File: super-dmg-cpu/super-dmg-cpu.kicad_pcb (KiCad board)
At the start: 2 copper layers, 83 x 78.5 mm, 61 parts, among them CN1 SCREEN, CN2 CART, CN3 BATTERY, CN4 BATTERY, P1 CART SHIELD GND PADS, P2 GND PAD, P3 GND PAD, P4 GND PAD, SW1 DPDT, U1 CPU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

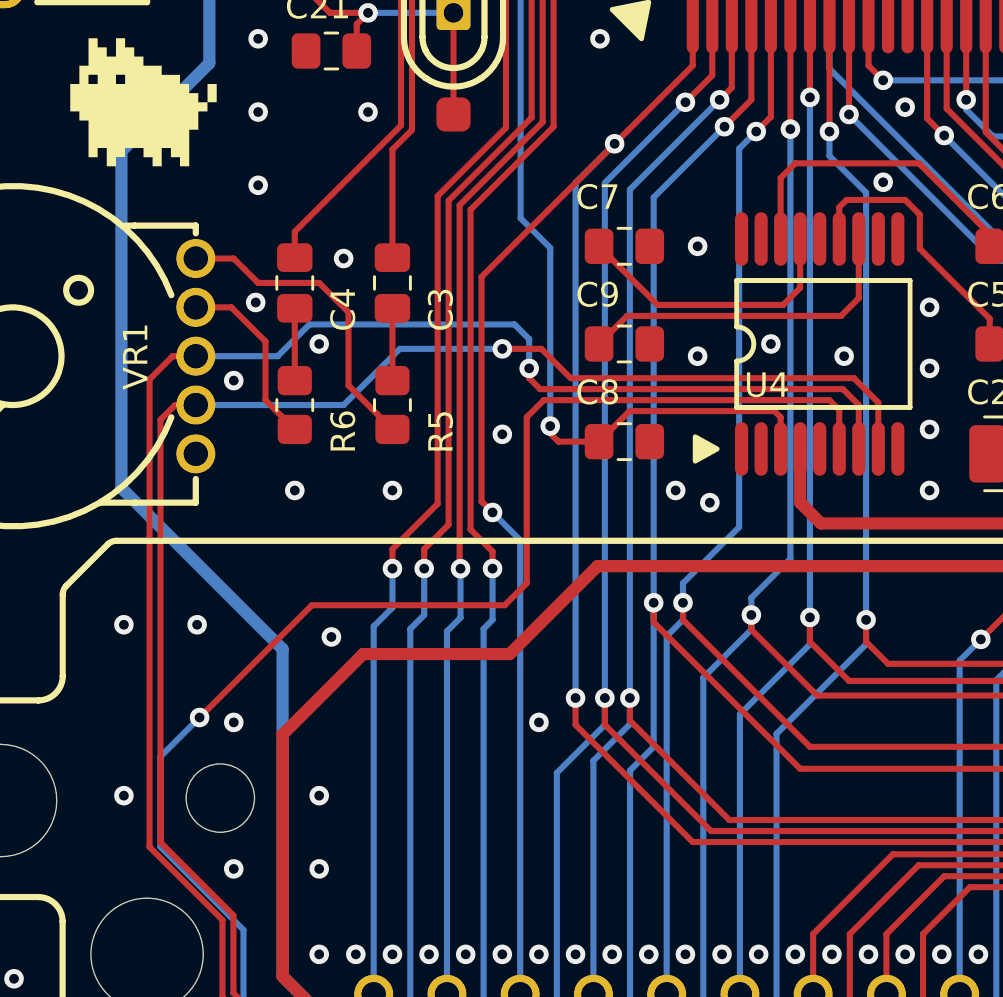
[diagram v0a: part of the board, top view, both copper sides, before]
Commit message: CPU: fix inverted L/R pins
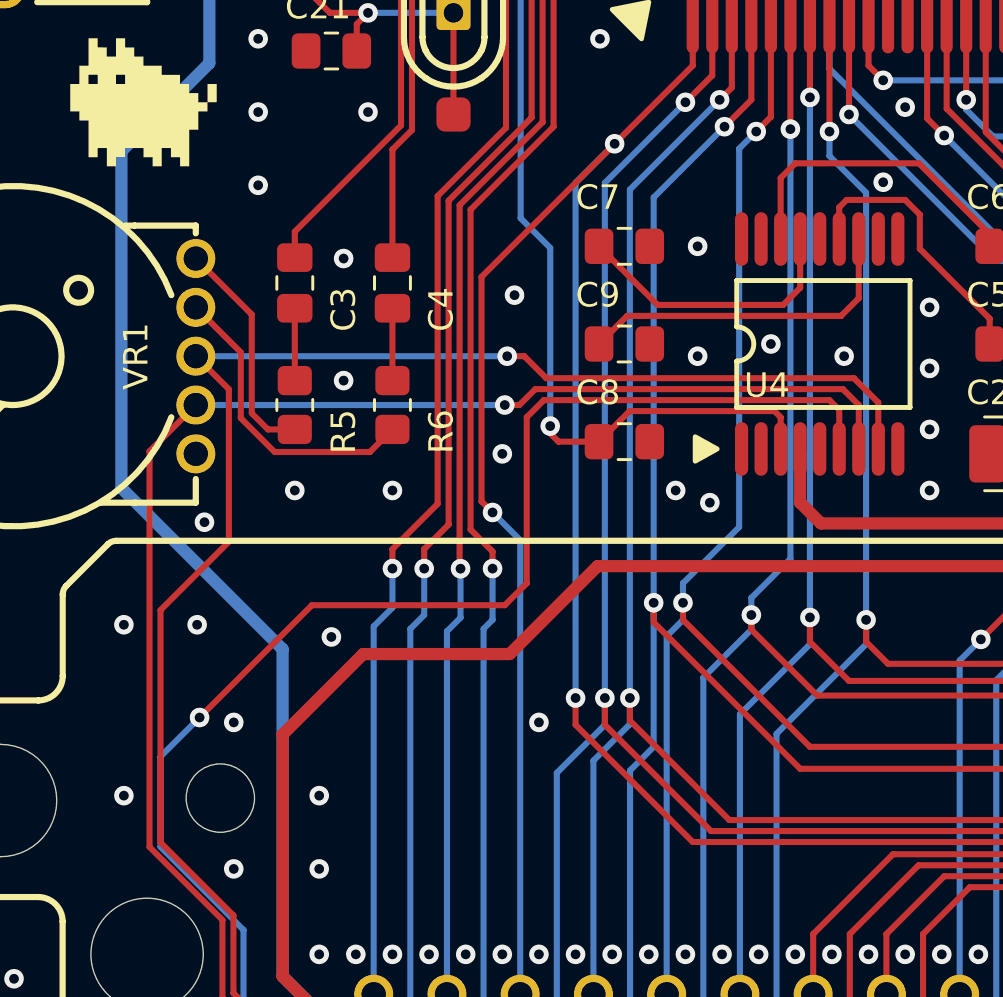
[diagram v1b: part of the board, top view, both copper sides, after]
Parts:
- moved C3 4.00 mm to (45.5, 67.5)
- moved C4 4.00 mm to (49.5, 67.5)
- moved R5 4.00 mm to (45.5, 72.5)
- moved R6 4.00 mm to (49.5, 72.5)
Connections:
- C3 pad 1: /LOUT -> /ROUT
- C4 pad 1: /ROUT -> /LOUT
- VR1 pad 2: /RPOT -> /LPOT
- VR1 pad 4: /LPOT -> /RPOT
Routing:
- net Net-(R6-Pad2): track 7.53 -> 12.5 mm
- net /RPOT: track 82.3 -> 77.5 mm
- net Net-(R5-Pad2): track 12.7 -> 9.32 mm
- net /LPOT: track 82.0 -> 83.5 mm

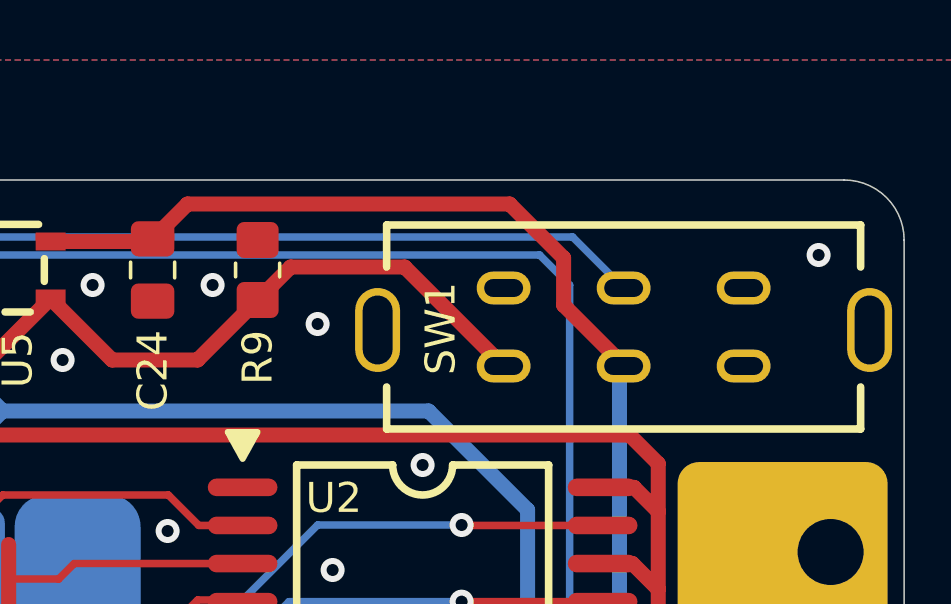
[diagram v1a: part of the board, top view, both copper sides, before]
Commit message: CPU: remove unused pads on the power switch
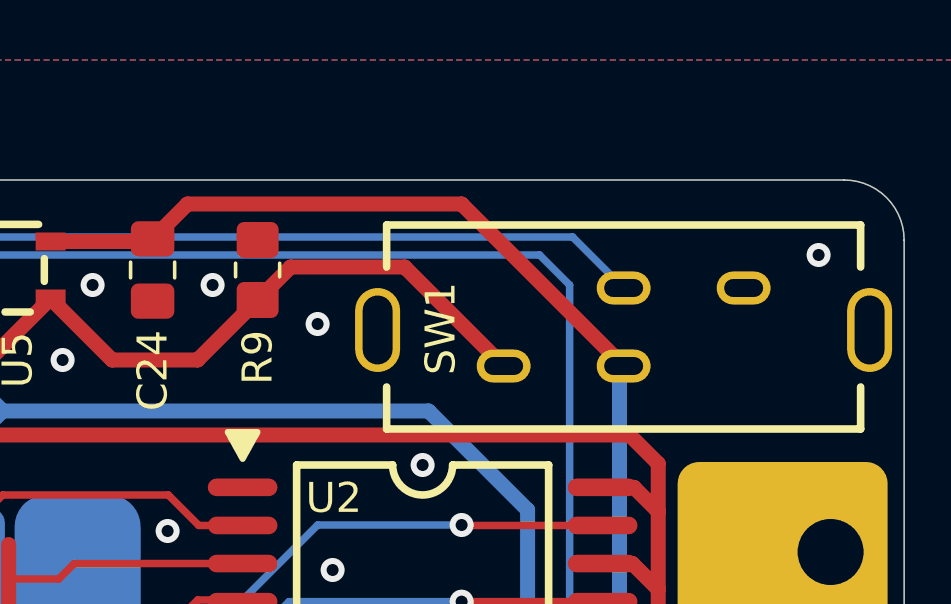
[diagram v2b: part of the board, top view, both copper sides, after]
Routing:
- net +BATT: track 182.2 -> 181.3 mm
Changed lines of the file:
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@@
   (net 109 "PD_OUT")
   (net 110 "unconnected-(U5-Pad3)")
-  (net 111 "unconnected-(SW1-Pad3)")
-  (net 112 "unconnected-(SW1-Pad4)")
-  (net 113 "Net-(D2-Pad1)")
+  (net 111 "Net-(D2-Pad1)")
   (footprint "dmg_lib:DMG_RAM_64K" locked (layer "F.Cu")
     (at 93.5 69.5)
@@
     (fp_line (start -5.5 -6.5) (end -5 -6.5) (layer "Dwgs.User") (width 0.254))
     (pad "1" thru_hole circle (at 0 -2.5) (size 1.4 1.4) (drill 0.8) (layers *.Mask "F.Cu" "In1.Cu" "B.Cu")
-      (net 113 "Net-(D2-Pad1)") (pinfunction "VDD") (pintype "passive"))
+      (net 111 "Net-(D2-Pad1)") (pinfunction "VDD") (pintype "passive"))
     (pad "2" thru_hole circle (at 2 -2.5) (size 1.4 1.4) (drill 0.8) (layers *.Mask "F.Cu" "In1.Cu" "B.Cu")
       (net 7 "/EXT_OUT") (pinfunction "SO") (pintype "passive"))
@@
     )
     (fp_line (start -7.9 -2.1) (end -7.9 -0.7) (layer "F.SilkS") (width 0.254))
-    (fp_line (start 7.9 -0.7) (end 7.9 -2.1) (layer "F.SilkS") (width 0.254))
-    (fp_line (start 7.9 -2.1) (end -7.9 -2.1) (layer "F.SilkS") (width 0.254))
     (fp_line (start -7.9 4.7) (end -7.9 3.3) (layer "F.SilkS") (width 0.254))
+    (fp_line (start 7.9 -2.1) (end -7.9 -2.1) (layer "F.SilkS") (width 0.254))
     (fp_line (start 7.9 4.7) (end 7.9 3.3) (layer "F.SilkS") (width 0.254))
+    (fp_line (start 7.9 -0.7) (end 7.9 -2.1) (layer "F.SilkS") (width 0.254))
     (fp_line (start -7.9 4.7) (end 7.9 4.7) (layer "F.SilkS") (width 0.254))
     (fp_line (start 5.4 -8.6) (end 5.4 -2.1) (layer "Dwgs.User") (width 0.25))
@@
     (pad "2" thru_hole oval locked (at 0 2.6) (size 1.8 1.1) (drill oval 1.3 0.6) (layers *.Cu *.Mask)
       (net 108 "+BATT") (pinfunction "VIN") (pintype "passive"))
-    (pad "3" thru_hole oval locked (at 4 2.6) (size 1.8 1.1) (drill oval 1.3 0.6) (layers *.Cu *.Mask)
-      (net 111 "unconnected-(SW1-Pad3)") (pinfunction "3") (pintype "no_connect"))
-    (pad "4" thru_hole oval locked (at -4 0) (size 1.8 1.1) (drill oval 1.3 0.6) (layers *.Cu *.Mask)
-      (net 112 "unconnected-(SW1-Pad4)") (pinfunction "4") (pintype "no_connect"))
     (pad "5" thru_hole oval locked (at 0 0) (size 1.8 1.1) (drill oval 1.3 0.6) (layers *.Cu *.Mask)
       (net 15 "/RST") (pinfunction "RST") (pintype "passive"))
     (pad "6" thru_hole oval locked (at 4 0) (size 1.8 1.1) (drill oval 1.3 0.6) (layers *.Cu *.Mask)
       (net 4 "GND") (pinfunction "GND") (pintype "passive"))
-    (pad "7" thru_hole oval locked (at 8.2 1.4 270) (size 2.8 1.5) (drill oval 2.3 1) (layers *.Cu *.Mask)
-      (net 4 "GND") (pinfunction "SH") (pintype "passive"))
     (pad "7" thru_hole oval locked (at -8.2 1.4 270) (size 2.8 1.5) (drill oval 2.3 1) (layers *.Cu *.Mask)
       (net 4 "GND") (pinfunction "SH") (pintype "passive"))
+    (pad "7" thru_hole oval locked (at 8.2 1.4 270) (size 2.8 1.5) (drill oval 2.3 1) (layers *.Cu *.Mask)
+      (net 4 "GND") (pinfunction "SH") (pintype "passive"))
   )
   (footprint "eda-glyphs:kmc_6mm" (layer "F.Cu")
@@
     (fp_line (start -1.4 -0.9) (end 1.4 -0.9) (layer "F.Fab") (width 0.1))
     (pad "1" smd rect (at -1.65 0 90) (size 0.9 1.2) (layers "F.Cu" "F.Paste" "F.Mask")
-      (net 113 "Net-(D2-Pad1)") (pinfunction "K") (pintype "passive"))
+      (net 111 "Net-(D2-Pad1)") (pinfunction "K") (pintype "passive"))
     (pad "2" smd rect (at 1.65 0 90) (size 0.9 1.2) (layers "F.Cu" "F.Paste" "F.Mask")
       (net 106 "+5V") (pinfunction "A") (pintype "passive"))
@@
     (fp_line (start -6 5) (end -5.031 5) (layer "F.SilkS") (width 0.254))
     (fp_arc (start -2.5 4) (mid -6.581538 -0.183962) (end -6 -6) (layer "F.SilkS") (width 0.254))
-    (fp_arc (start 6 -6) (mid 6.581539 -0.183962) (end 2.5 4) (layer "F.SilkS") (width 0.254))
+    (fp_arc (start 6 -6) (mid 6.581539 -0.183961) (end 2.5 4) (layer "F.SilkS") (width 0.254))
     (fp_arc (start -3.199638 -4.100525) (mid -3.096245 -5.695327) (end -1.501 -5.599) (layer "F.SilkS") (width 0.254))
     (fp_circle (center 0 -2.5) (end 2 -2.5) (layer "F.SilkS") (width 0.254) (fill none))
@@
   (segment (start 73.6 32) (end 79.55 32) (width 0.5) (layer "F.Cu") (net 107))
   (segment (start 32.05 101.35) (end 32.05 100) (width 0.5) (layer "F.Cu") (net 108))
-  (segment (start 98.7 28.6) (end 96.9 26.8) (width 0.5) (layer "F.Cu") (net 108))
   (segment (start 73.69 101.6) (end 71.297501 103.992499) (width 0.5) (layer "F.Cu") (net 108))
   (segment (start 102.525489 103.849511) (end 104.775 101.6) (width 0.5) (layer "F.Cu") (net 108))
-  (segment (start 96.9 26.8) (end 86.1625 26.8) (width 0.5) (layer "F.Cu") (net 108))
+  (segment (start 95.3 26.8) (end 86.1625 26.8) (width 0.5) (layer "F.Cu") (net 108))
   (segment (start 89.846569 102.742979) (end 88.576548 104.013) (width 0.5) (layer "F.Cu") (net 108))
-  (segment (start 86.1625 26.8) (end 85 27.9625) (width 0.5) (layer "F.Cu") (net 108))
+  (segment (start 100.668639 32.168639) (end 95.3 26.8) (width 0.5) (layer "F.Cu") (net 108))
   (segment (start 95.049547 102.742979) (end 96.156079 103.849511) (width 0.5) (layer "F.Cu") (net 108))
   (segment (start 92.436116 102.742979) (end 95.049547 102.742979) (width 0.5) (layer "F.Cu") (net 108))
+  (segment (start 86.1625 26.8) (end 85 27.9625) (width 0.5) (layer "F.Cu") (net 108))
   (segment (start 34.692499 103.992499) (end 32.05 101.35) (width 0.5) (layer "F.Cu") (net 108))
   (segment (start 76.103 104.013) (end 73.69 101.6) (width 0.5) (layer "F.Cu") (net 108))
   (segment (start 71.297501 103.992499) (end 34.692499 103.992499) (width 0.5) (layer "F.Cu") (net 108))
-  (segment (start 100.668639 32.139193) (end 98.7 30.170554) (width 0.5) (layer "F.Cu") (net 108))
-  (segment (start 98.7 30.170554) (end 98.7 28.6) (width 0.5) (layer "F.Cu") (net 108))
   (segment (start 81.6 28.05) (end 84.9125 28.05) (width 0.5) (layer "F.Cu") (net 108))
   (segment (start 92.436116 102.742979) (end 89.846569 102.742979) (width 0.5) (layer "F.Cu") (net 108))
+  (segment (start 100.668639 32.139193) (end 100.668639 32.168639) (width 0.5) (layer "F.Cu") (net 108))
   (segment (start 88.576548 104.013) (end 76.103 104.013) (width 0.5) (layer "F.Cu") (net 108))
   (segment (start 96.156079 103.849511) (end 102.525489 103.849511) (width 0.5) (layer "F.Cu") (net 108))
@@
   (segment (start 78 30.9) (end 78 31.7) (width 0.5) (layer "B.Cu") (net 109))
   (segment (start 97.5 37) (end 94.2 33.7) (width 0.5) (layer "B.Cu") (net 109))
-  (segment (start 35.95 47) (end 34.2 48.75) (width 0.25) (layer "F.Cu") (net 113))
-  (segment (start 34.2 48.75) (end 34.2 53.3) (width 0.25) (layer "F.Cu") (net 113))
-  (segment (start 36.05 55.15) (end 42 55.15) (width 0.25) (layer "F.Cu") (net 113))
-  (segment (start 34.2 53.3) (end 36.05 55.15) (width 0.25) (layer "F.Cu") (net 113))
+  (segment (start 35.95 47) (end 34.2 48.75) (width 0.25) (layer "F.Cu") (net 111))
+  (segment (start 34.2 48.75) (end 34.2 53.3) (width 0.25) (layer "F.Cu") (net 111))
+  (segment (start 36.05 55.15) (end 42 55.15) (width 0.25) (layer "F.Cu") (net 111))
+  (segment (start 34.2 53.3) (end 36.05 55.15) (width 0.25) (layer "F.Cu") (net 111))
   (zone (net 0) (net_name "") (layer "F.Cu") (hatch edge 0.508)
     (connect_pads (clearance 0))
